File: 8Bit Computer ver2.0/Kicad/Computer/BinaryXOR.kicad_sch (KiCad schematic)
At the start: 4 parts, among them IC1 SN74ABT821ADWR, IC2 SN74HCS74DR, IC3 SN74LVC1G14DBVR, IC4 SN74HCS86DR

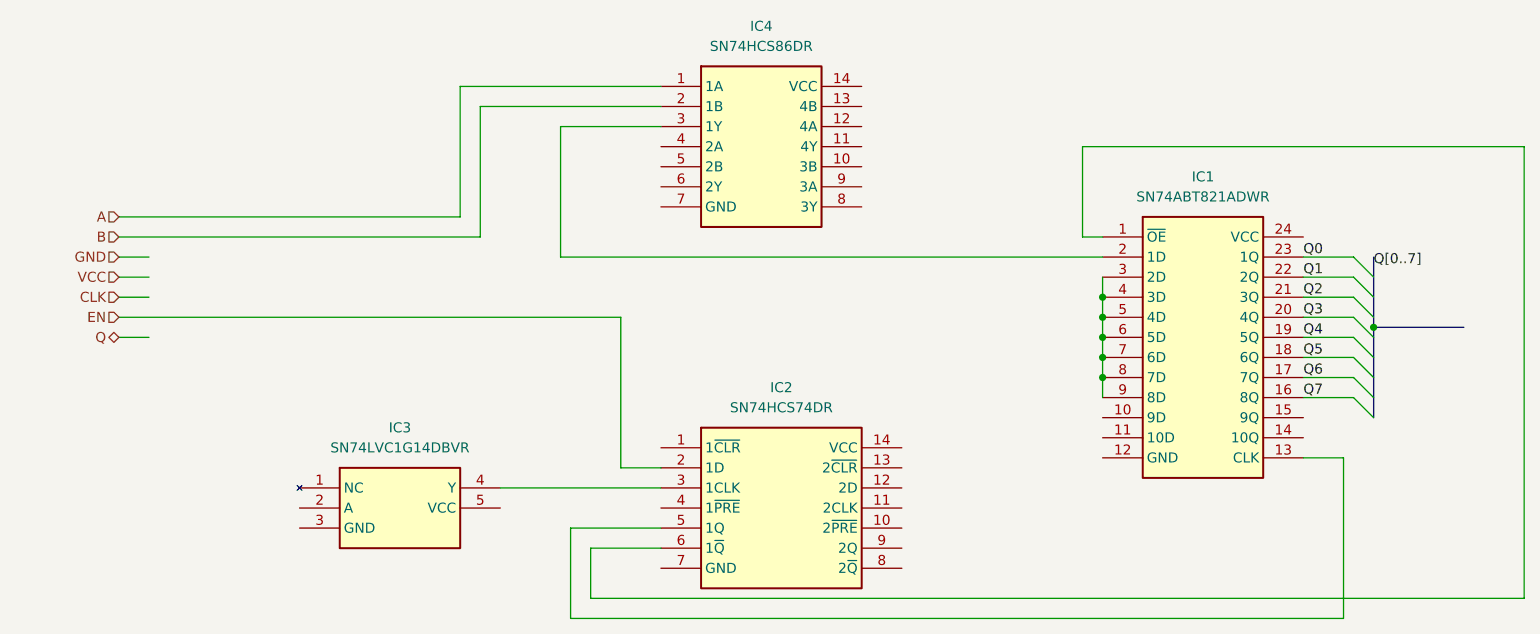
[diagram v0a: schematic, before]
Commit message: parts,Kicad
added 74HCS574 to Kicad
Kicad:
ALU->added Bitwise NOT,OR,XOR,AND
ALU->added A,B 8in OR
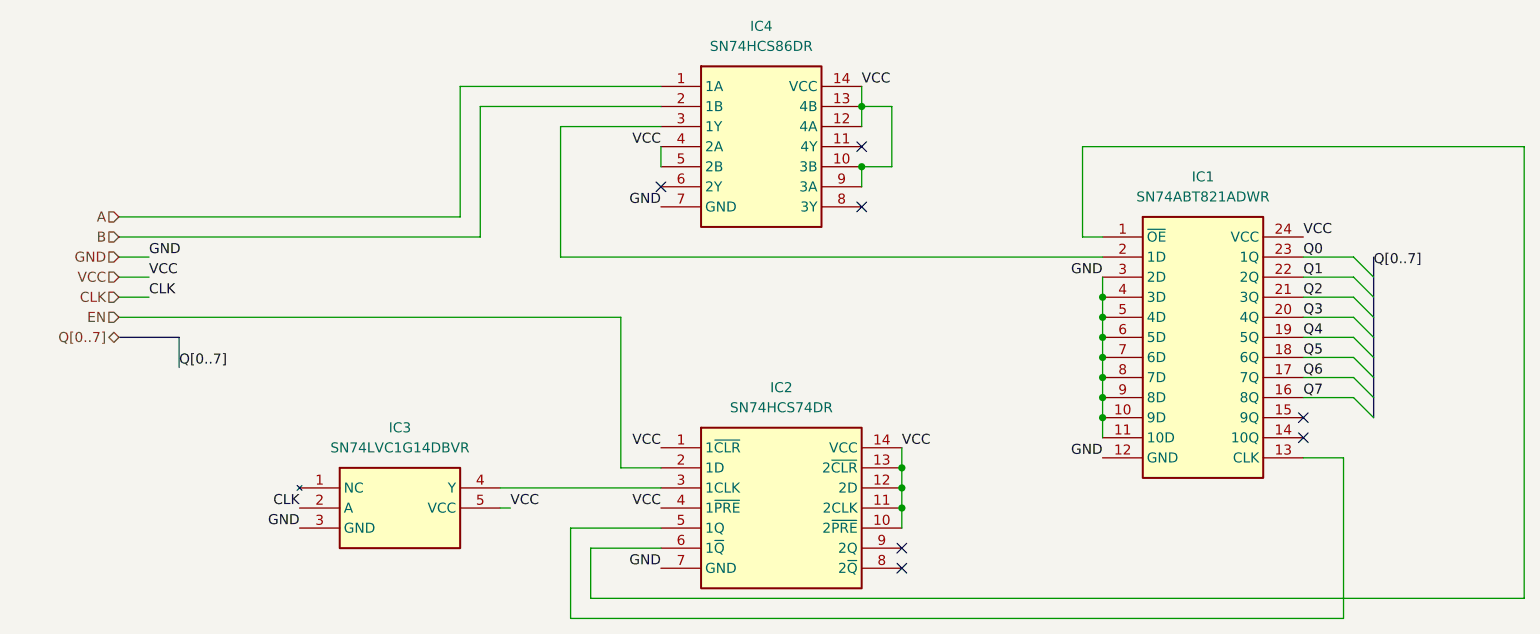
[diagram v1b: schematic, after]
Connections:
- net CLK: now also IC3.2 (A)
- net GND: now also IC1.10 (9D), IC1.11 (10D), IC1.12 (GND), IC1.3 (2D), IC1.4 (3D), IC1.5 (4D), IC1.6 (5D), IC1.7 (6D), IC1.8 (7D), IC1.9 (8D), IC2.7 (GND), IC3.3 (GND), IC4.7 (GND)
- net VCC: now also IC1.24 (VCC), IC2.1 (1~{CLR}), IC2.10 (2~{PRE}), IC2.11 (2CLK), IC2.12 (2D), IC2.13 (2~{CLR}), IC2.14 (VCC), IC2.4 (1~{PRE}), IC3.5 (VCC), IC4.10 (3B), IC4.12 (4A), IC4.13 (4B), IC4.14 (VCC), IC4.4 (2A), IC4.5 (2B), IC4.9 (3A)
- no-connect marks 0 -> 7

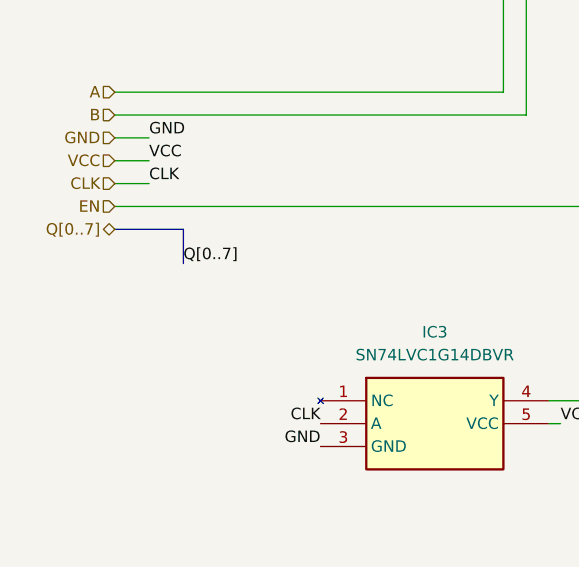
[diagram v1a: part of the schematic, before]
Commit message: Kicad,parts
Kicad:
added FlagRegister
began Inc, Comp
parts:
added comparator for P>Q 682
added faster sram 12ns AS7C
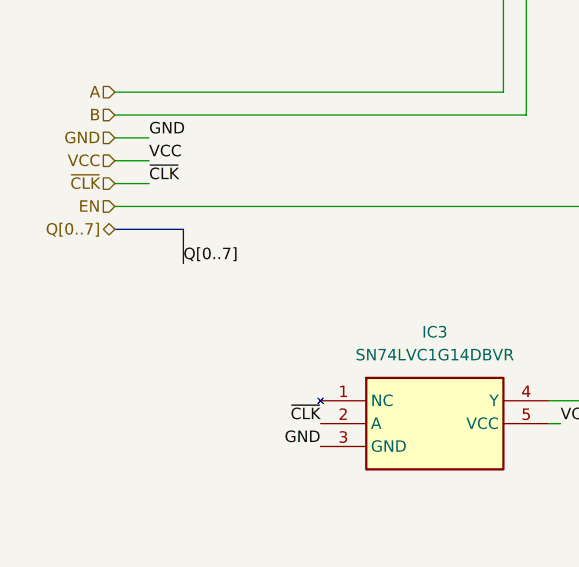
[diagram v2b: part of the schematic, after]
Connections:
- net CLK renamed ~{CLK}
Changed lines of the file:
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@@
 		)
 	)
-	(label "CLK"
+	(label "~{CLK}"
 		(at 48.26 106.68 180)
 		(effects
@@
 		)
 	)
-	(label "CLK"
+	(label "~{CLK}"
 		(at 29.21 80.01 0)
 		(effects
@@
 		)
 	)
-	(hierarchical_label "CLK"
+	(hierarchical_label "~{CLK}"
 		(shape input)
 		(at 25.4 80.01 180)

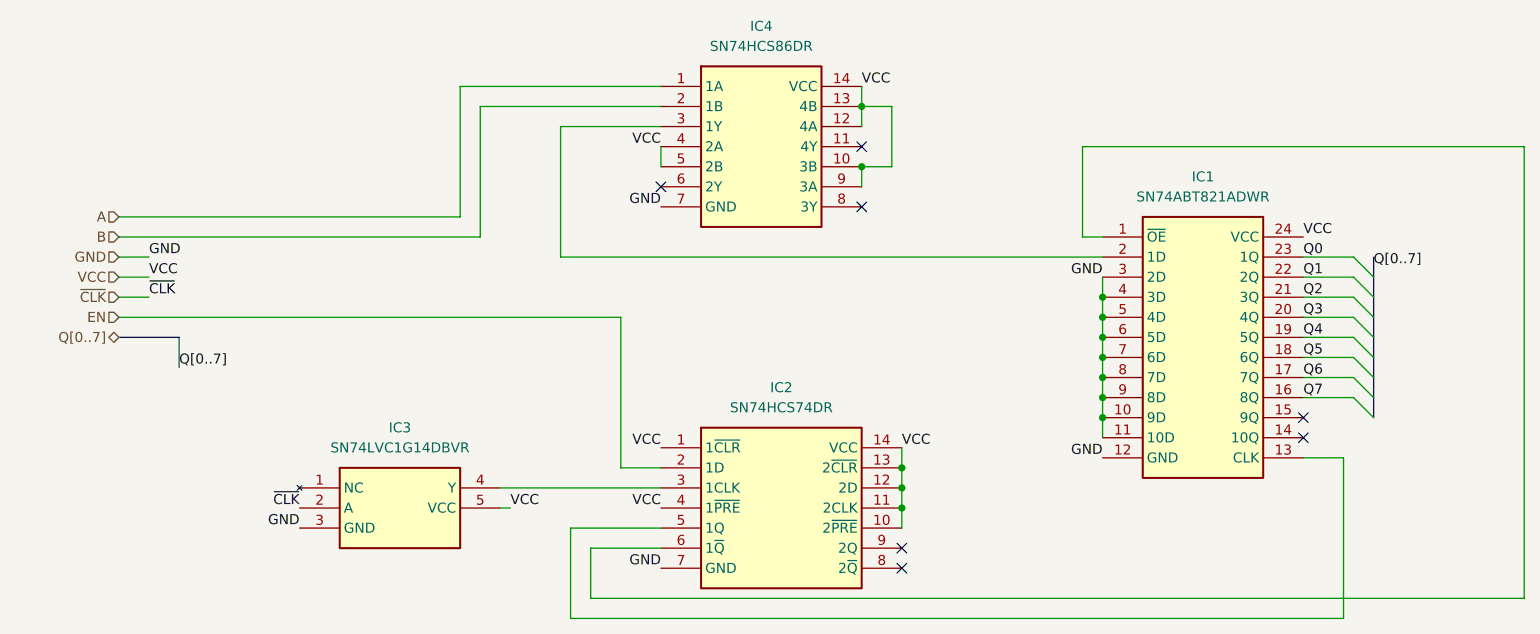
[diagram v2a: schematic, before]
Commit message: parts,Kicad
parts:
changed 8xDlatch HCS to ABT 574
waiting for SRAM CAD Model
Kicad:
imported AHC types of ICs
added ProgrammeCounter
finished Comparator
changed all HCS to AHC except 3in OR ->no AHC Version
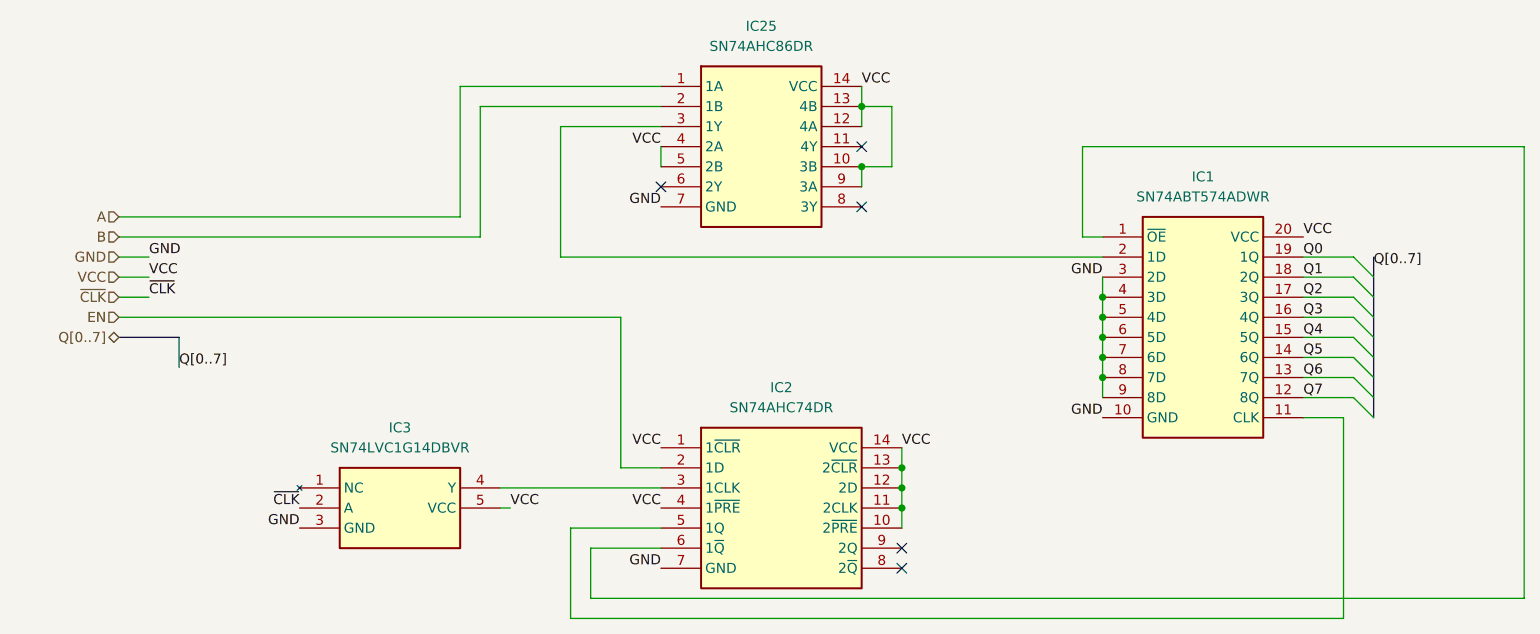
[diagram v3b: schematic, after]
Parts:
- removed IC1: SN74ABT821ADWR, Samacsys:SOIC127P1030X265-24N, symbol Samacsys:SN74ABT821ADWR
- removed IC2: SN74HCS74DR, Samacsys:SOIC127P600X175-14N, symbol Samacsys:SN74HCS74DR
- removed IC4: SN74HCS86DR, Samacsys:SOIC127P600X175-14N, symbol Samacsys:SN74HCS86DR
- added IC1: SN74ABT574ADWR, Samacsys:SOIC127P1030X265-20N, symbol Samacsys:SN74ABT574ADWR
- added IC2: SN74AHC74DR, Samacsys:SOIC127P600X175-14N, symbol Samacsys:SN74AHC74DR
- added IC25: SN74AHC86DR, Samacsys:SOIC127P600X175-14N, symbol Samacsys:SN74AHC86DR
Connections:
- net A: now also IC25.1 (1A)
- net B: now also IC25.2 (1B)
- net EN: now also IC2.2 (1D)
- net GND: now also IC1.10 (GND), IC1.3 (2D), IC1.4 (3D), IC1.5 (4D), IC1.6 (5D), IC1.7 (6D), IC1.8 (7D), IC1.9 (8D), IC2.7 (GND), IC25.7 (GND)
- net Q0: now also IC1.19 (1Q)
- net Q1: now also IC1.18 (2Q)
- net Q2: now also IC1.17 (3Q)
- net Q3: now also IC1.16 (4Q)
- net Q4: now also IC1.15 (5Q)
- net Q5: now also IC1.14 (6Q)
- net Q6: now also IC1.13 (7Q)
- net Q7: now also IC1.12 (8Q)
- net VCC: now also IC1.20 (VCC), IC2.1 (1~{CLR}), IC2.10 (2~{PRE}), IC2.11 (2CLK), IC2.12 (2D), IC2.13 (2~{CLR}), IC2.14 (VCC), IC2.4 (1~{PRE}), IC25.10 (3B), IC25.12 (4A), IC25.13 (4B), IC25.14 (VCC), IC25.4 (2A), IC25.5 (2B), IC25.9 (3A)
- net at IC3.4 (Y): now also IC2.3 (1CLK)
- new net: IC1.2 (1D), IC25.3 (1Y)
- new net: IC1.11 (CLK), IC2.5 (1Q)
- new net: IC1.1 (~{OE}), IC2.6 (1~{Q})
- no-connect marks 7 -> 5

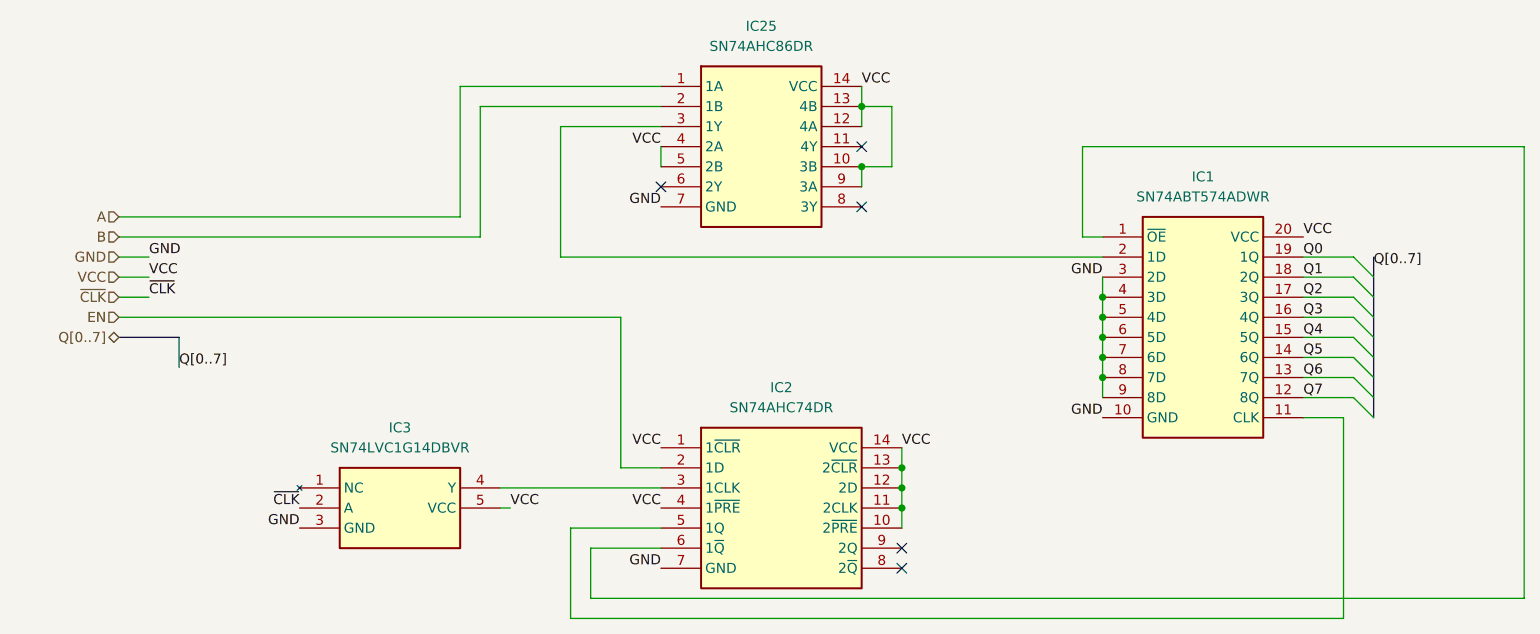
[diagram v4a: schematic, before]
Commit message: Kicad, parts
Parts:
added Leds
Kicad:
added Input Output
changed Q bus to DAT bus
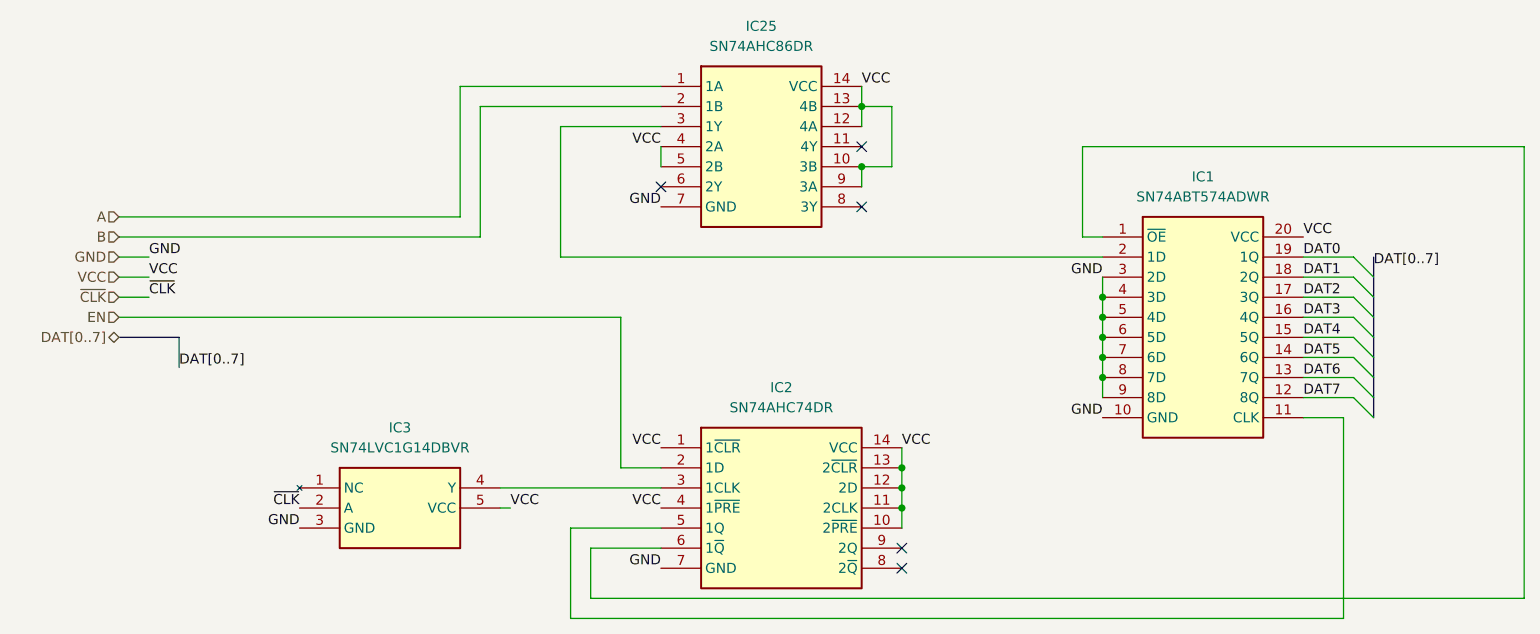
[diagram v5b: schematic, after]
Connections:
- net Q0 renamed DAT0
- net Q1 renamed DAT1
- net Q2 renamed DAT2
- net Q3 renamed DAT3
- net Q4 renamed DAT4
- net Q5 renamed DAT5
- net Q6 renamed DAT6
- net Q7 renamed DAT7
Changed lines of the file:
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@@
 		)
 	)
-	(label "Q[0..7]"
+	(label "DAT[0..7]"
 		(at 33.02 88.9 0)
 		(effects
@@
 		)
 	)
-	(label "Q6"
+	(label "DAT6"
 		(at 175.26 90.17 0)
 		(effects
@@
 		)
 	)
-	(label "Q4"
+	(label "DAT4"
 		(at 175.26 85.09 0)
 		(effects
@@
 		)
 	)
-	(label "Q3"
+	(label "DAT3"
 		(at 175.26 82.55 0)
 		(effects
@@
 		)
 	)
-	(label "Q7"
+	(label "DAT7"
 		(at 175.26 92.71 0)
 		(effects
@@
 		)
 	)
-	(label "Q1"
+	(label "DAT1"
 		(at 175.26 77.47 0)
 		(effects
@@
 		)
 	)
-	(label "Q[0..7]"
+	(label "DAT[0..7]"
 		(at 184.15 76.2 0)
 		(effects
@@
 		)
 	)
-	(label "Q2"
+	(label "DAT2"
 		(at 175.26 80.01 0)
 		(effects
@@
 		)
 	)
-	(label "Q0"
+	(label "DAT0"
 		(at 175.26 74.93 0)
 		(effects
@@
 		)
 	)
-	(label "Q5"
+	(label "DAT5"
 		(at 175.26 87.63 0)
 		(effects
@@
 		)
 	)
-	(hierarchical_label "Q[0..7]"
+	(hierarchical_label "DAT[0..7]"
 		(shape tri_state)
 		(at 25.4 85.09 180)

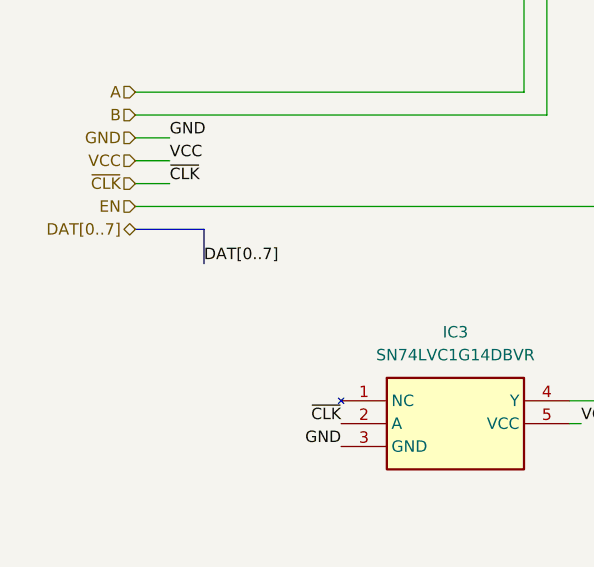
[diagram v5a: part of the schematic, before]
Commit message: Kicad, parts
parts:
added USB C PD Triggerboard
added Delay Chip for 90ns
added Push Button
Kicad:
added USB C PD Triggerboard
added rising edge detector via Delay and Xor for Accept Push Button
added VBUS net
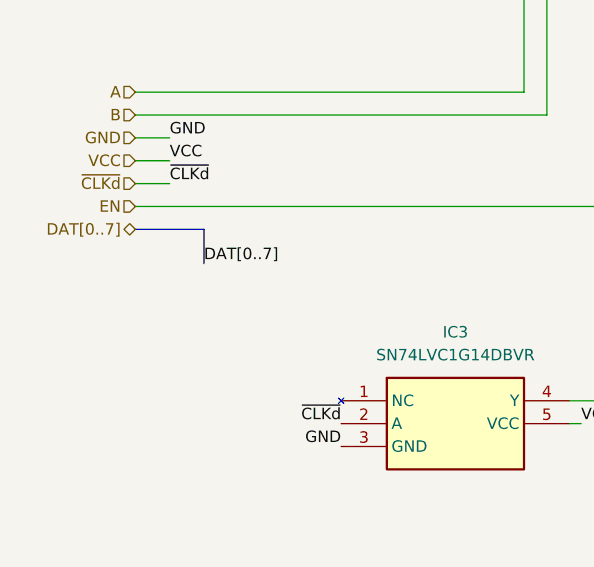
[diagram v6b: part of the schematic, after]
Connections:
- net ~{CLK} renamed ~{CLKd}
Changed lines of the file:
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@@
 		)
 	)
-	(label "~{CLK}"
+	(label "~{CLKd}"
 		(at 48.26 106.68 180)
 		(effects
@@
 		)
 	)
-	(label "~{CLK}"
+	(label "~{CLKd}"
 		(at 29.21 80.01 0)
 		(effects
@@
 		)
 	)
-	(hierarchical_label "~{CLK}"
+	(hierarchical_label "~{CLKd}"
 		(shape input)
 		(at 25.4 80.01 180)
